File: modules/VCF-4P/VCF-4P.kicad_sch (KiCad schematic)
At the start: 40 parts, among them U1 SSI2140, U2 TL074

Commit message: VCF-4P: change a footprint
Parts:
- U1: footprint Package_SO:SSOP-20_4.4x6.5mm_P0.65mm -> (none)
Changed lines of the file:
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@@
       (effects (font (size 1.27 1.27)) hide)
     )
+    (pin "1")
+    (pin "2")
+    (pin "3")
+    (pin "5")
+    (pin "6")
+    (pin "7")
+    (pin "10")
+    (pin "8")
+    (pin "9")
     (pin "12")
     (pin "13")
     (pin "14")
+    (pin "11")
+    (pin "4")
   )
   (symbol (lib_id "-lmp:R_1%_0W166") (at 175.26 52.07 0) (unit 1)
@@
       (effects (font (size 1.27 1.27)) hide)
     )
+    (pin "1")
+    (pin "2")
+    (pin "3")
     (pin "5")
     (pin "6")
     (pin "7")
+    (pin "10")
+    (pin "8")
+    (pin "9")
+    (pin "12")
+    (pin "13")
+    (pin "14")
+    (pin "11")
+    (pin "4")
   )
   (symbol (lib_name "SSI2140_1") (lib_id "-lmp-synth:SSI2140") (at 106.68 152.4 0) (unit 6)
@@
       (effects (font (size 1.27 1.27)) (justify right))
     )
-    (property "Footprint" "Package_SO:SSOP-20_4.4x6.5mm_P0.65mm" (id 2) (at 112.395 141.605 0)
+    (property "Footprint" "" (id 2) (at 112.395 141.605 0)
       (effects (font (size 1.27 1.27)) hide)
     )
@@
       (effects (font (size 1.27 1.27)) hide)
     )
+    (pin "4")
+    (pin "5")
+    (pin "6")
+    (pin "1")
+    (pin "2")
+    (pin "3")
+    (pin "17")
+    (pin "18")
+    (pin "19")
+    (pin "14")
+    (pin "15")
+    (pin "16")
+    (pin "12")
+    (pin "13")
+    (pin "9")
     (pin "10")
     (pin "11")
@@
     (property "Reference" "U1" (id 0) (at 115.57 30.6664 0))
     (property "Value" "SSI2140" (id 1) (at 115.57 33.2033 0))
-    (property "Footprint" "Package_SO:SSOP-20_4.4x6.5mm_P0.65mm" (id 2) (at 120.015 28.575 0)
+    (property "Footprint" "" (id 2) (at 120.015 28.575 0)
       (effects (font (size 1.27 1.27)) hide)
     )
@@
     (pin "5")
     (pin "6")
+    (pin "1")
+    (pin "2")
+    (pin "3")
+    (pin "17")
+    (pin "18")
+    (pin "19")
+    (pin "14")
+    (pin "15")
+    (pin "16")
+    (pin "12")
+    (pin "13")
+    (pin "9")
+    (pin "10")
+    (pin "11")
+    (pin "20")
+    (pin "7")
+    (pin "8")
   )
   (symbol (lib_id "-lmp:R_1%_0W166") (at 91.44 52.07 0) (unit 1)
@@
     (property "Reference" "U1" (id 0) (at 189.23 30.6664 0))
     (property "Value" "SSI2140" (id 1) (at 189.23 33.2033 0))
-    (property "Footprint" "Package_SO:SSOP-20_4.4x6.5mm_P0.65mm" (id 2) (at 193.675 28.575 0)
+    (property "Footprint" "" (id 2) (at 193.675 28.575 0)
       (effects (font (size 1.27 1.27)) hide)
     )
@@
       (effects (font (size 1.27 1.27)) hide)
     )
+    (pin "4")
+    (pin "5")
+    (pin "6")
+    (pin "1")
+    (pin "2")
+    (pin "3")
     (pin "17")
     (pin "18")
     (pin "19")
+    (pin "14")
+    (pin "15")
+    (pin "16")
+    (pin "12")
+    (pin "13")
+    (pin "9")
+    (pin "10")
+    (pin "11")
+    (pin "20")
+    (pin "7")
+    (pin "8")
   )
   (symbol (lib_id "-lmp-synth:SSI2140") (at 151.13 39.37 0) (unit 2)
@@
     (property "Reference" "U1" (id 0) (at 152.4 30.6664 0))
     (property "Value" "SSI2140" (id 1) (at 152.4 33.2033 0))
-    (property "Footprint" "Package_SO:SSOP-20_4.4x6.5mm_P0.65mm" (id 2) (at 156.845 28.575 0)
+    (property "Footprint" "" (id 2) (at 156.845 28.575 0)
       (effects (font (size 1.27 1.27)) hide)
     )
@@
       (effects (font (size 1.27 1.27)) hide)
     )
+    (pin "4")
+    (pin "5")
+    (pin "6")
     (pin "1")
     (pin "2")
     (pin "3")
+    (pin "17")
+    (pin "18")
+    (pin "19")
+    (pin "14")
+    (pin "15")
+    (pin "16")
+    (pin "12")
+    (pin "13")
+    (pin "9")
+    (pin "10")
+    (pin "11")
+    (pin "20")
+    (pin "7")
+    (pin "8")
   )
   (symbol (lib_id "-lmp:R_1%_0W166") (at 138.43 52.07 0) (unit 1)
@@
     (property "Reference" "U1" (id 0) (at 101.6 66.1502 0))
     (property "Value" "SSI2140" (id 1) (at 101.6 68.6871 0))
-    (property "Footprint" "Package_SO:SSOP-20_4.4x6.5mm_P0.65mm" (id 2) (at 106.045 64.135 0)
+    (property "Footprint" "" (id 2) (at 106.045 64.135 0)
       (effects (font (size 1.27 1.27)) hide)
     )
@@
       (effects (font (size 1.27 1.27)) hide)
     )
+    (pin "4")
+    (pin "5")
+    (pin "6")
+    (pin "1")
+    (pin "2")
+    (pin "3")
+    (pin "17")
+    (pin "18")
+    (pin "19")
+    (pin "14")
+    (pin "15")
+    (pin "16")
     (pin "12")
     (pin "13")
     (pin "9")
+    (pin "10")
+    (pin "11")
+    (pin "20")
+    (pin "7")
+    (pin "8")
   )
   (symbol (lib_id "-lmp-power:GND") (at 212.09 57.15 0) (unit 1)
@@
     (property "Reference" "U1" (id 0) (at 226.06 30.6664 0))
     (property "Value" "SSI2140" (id 1) (at 226.06 33.2033 0))
-    (property "Footprint" "Package_SO:SSOP-20_4.4x6.5mm_P0.65mm" (id 2) (at 230.505 28.575 0)
+    (property "Footprint" "" (id 2) (at 230.505 28.575 0)
       (effects (font (size 1.27 1.27)) hide)
     )
@@
       (effects (font (size 1.27 1.27)) hide)
     )
+    (pin "4")
+    (pin "5")
+    (pin "6")
+    (pin "1")
+    (pin "2")
+    (pin "3")
+    (pin "17")
+    (pin "18")
+    (pin "19")
     (pin "14")
     (pin "15")
     (pin "16")
+    (pin "12")
+    (pin "13")
+    (pin "9")
+    (pin "10")
+    (pin "11")
+    (pin "20")
+    (pin "7")
+    (pin "8")
   )
   (symbol (lib_id "-lmp-opamp:TL074") (at 67.31 152.4 0) (mirror x) (unit 3)
@@
       (effects (font (size 1.27 1.27)) hide)
     )
+    (pin "1")
+    (pin "2")
+    (pin "3")
+    (pin "5")
+    (pin "6")
+    (pin "7")
     (pin "10")
     (pin "8")
     (pin "9")
+    (pin "12")
+    (pin "13")
+    (pin "14")
+    (pin "11")
+    (pin "4")
   )
   (symbol (lib_id "-lmp-synth:R_1K_Output") (at 222.25 102.87 90) (unit 1)
@@
     (pin "2")
     (pin "3")
+    (pin "5")
+    (pin "6")
+    (pin "7")
+    (pin "10")
+    (pin "8")
+    (pin "9")
+    (pin "12")
+    (pin "13")
+    (pin "14")
+    (pin "11")
+    (pin "4")
   )
   (symbol (lib_id "-lmp-power:GND") (at 58.42 157.48 0) (unit 1)
@@
     )
     (path "/35af1613-5429-4d36-8b84-d4f2f54bd286"
-      (reference "U1") (unit 1) (value "SSI2140") (footprint "Package_SO:SSOP-20_4.4x6.5mm_P0.65mm")
+      (reference "U1") (unit 1) (value "SSI2140") (footprint "-lmp-breakout:Breakout_DIP-20_W15.24mm")
     )
     (path "/7b9141a7-0442-4e17-91fc-6134d64028ce"
-      (reference "U1") (unit 2) (value "SSI2140") (footprint "Package_SO:SSOP-20_4.4x6.5mm_P0.65mm")
+      (reference "U1") (unit 2) (value "SSI2140") (footprint "-lmp-breakout:Breakout_DIP-20_W15.24mm")
     )
     (path "/799ca06d-feeb-42b5-93f5-6141a9976a1b"
-      (reference "U1") (unit 3) (value "SSI2140") (footprint "Package_SO:SSOP-20_4.4x6.5mm_P0.65mm")
+      (reference "U1") (unit 3) (value "SSI2140") (footprint "-lmp-breakout:Breakout_DIP-20_W15.24mm")
     )
     (path "/9773e1b2-867f-4bba-aab9-6aa389e51a1c"
-      (reference "U1") (unit 4) (value "SSI2140") (footprint "Package_SO:SSOP-20_4.4x6.5mm_P0.65mm")
+      (reference "U1") (unit 4) (value "SSI2140") (footprint "-lmp-breakout:Breakout_DIP-20_W15.24mm")
     )
     (path "/9131ee65-f6a7-4f4e-a019-faa937da667b"
-      (reference "U1") (unit 5) (value "SSI2140") (footprint "Package_SO:SSOP-20_4.4x6.5mm_P0.65mm")
+      (reference "U1") (unit 5) (value "SSI2140") (footprint "-lmp-breakout:Breakout_DIP-20_W15.24mm")
     )
     (path "/15b8c170-a65b-4a6d-a943-e95b801e6cde"
-      (reference "U1") (unit 6) (value "SSI2140") (footprint "Package_SO:SSOP-20_4.4x6.5mm_P0.65mm")
+      (reference "U1") (unit 6) (value "SSI2140") (footprint "-lmp-breakout:Breakout_DIP-20_W15.24mm")
     )
     (path "/d485a6e6-3ae5-4c97-8cc2-20d463f5a713"

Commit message: VCF-4P: input level uses audio-taper pot
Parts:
- U1: footprint (none) -> -lmp-breakout:Breakout_DIP-20_W15.24mm
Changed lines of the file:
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@@
       (effects (font (size 1.27 1.27)) (justify right))
     )
-    (property "Footprint" "" (id 2) (at 112.395 141.605 0)
+    (property "Footprint" "-lmp-breakout:Breakout_DIP-20_W15.24mm" (id 2) (at 112.395 141.605 0)
       (effects (font (size 1.27 1.27)) hide)
     )
@@
     (property "Reference" "U1" (id 0) (at 115.57 30.6664 0))
     (property "Value" "SSI2140" (id 1) (at 115.57 33.2033 0))
-    (property "Footprint" "" (id 2) (at 120.015 28.575 0)
+    (property "Footprint" "-lmp-breakout:Breakout_DIP-20_W15.24mm" (id 2) (at 120.015 28.575 0)
       (effects (font (size 1.27 1.27)) hide)
     )
@@
     (property "Reference" "U1" (id 0) (at 189.23 30.6664 0))
     (property "Value" "SSI2140" (id 1) (at 189.23 33.2033 0))
-    (property "Footprint" "" (id 2) (at 193.675 28.575 0)
+    (property "Footprint" "-lmp-breakout:Breakout_DIP-20_W15.24mm" (id 2) (at 193.675 28.575 0)
       (effects (font (size 1.27 1.27)) hide)
     )
@@
     (property "Reference" "U1" (id 0) (at 152.4 30.6664 0))
     (property "Value" "SSI2140" (id 1) (at 152.4 33.2033 0))
-    (property "Footprint" "" (id 2) (at 156.845 28.575 0)
+    (property "Footprint" "-lmp-breakout:Breakout_DIP-20_W15.24mm" (id 2) (at 156.845 28.575 0)
       (effects (font (size 1.27 1.27)) hide)
     )
@@
     (property "Reference" "U1" (id 0) (at 101.6 66.1502 0))
     (property "Value" "SSI2140" (id 1) (at 101.6 68.6871 0))
-    (property "Footprint" "" (id 2) (at 106.045 64.135 0)
+    (property "Footprint" "-lmp-breakout:Breakout_DIP-20_W15.24mm" (id 2) (at 106.045 64.135 0)
       (effects (font (size 1.27 1.27)) hide)
     )
@@
     (property "Reference" "U1" (id 0) (at 226.06 30.6664 0))
     (property "Value" "SSI2140" (id 1) (at 226.06 33.2033 0))
-    (property "Footprint" "" (id 2) (at 230.505 28.575 0)
-      (effects (font (size 1.27 1.27)) hide)
-    )
+    (property "Footprint" "-lmp-breakout:Breakout_DIP-20_W15.24mm" (id 2) (at 230.505 28.575 0)
+      (effects (font (size 1.27 1.27)) hide)
+    )

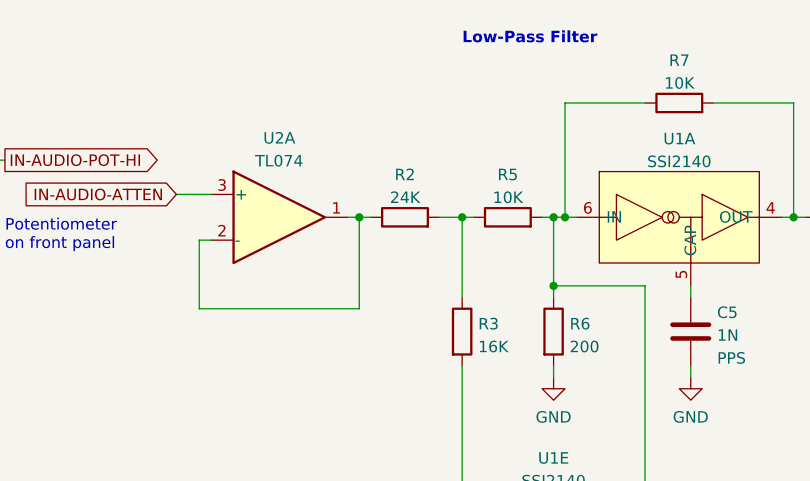
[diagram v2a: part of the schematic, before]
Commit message: VCF-4P: Breadboard prototype - wip
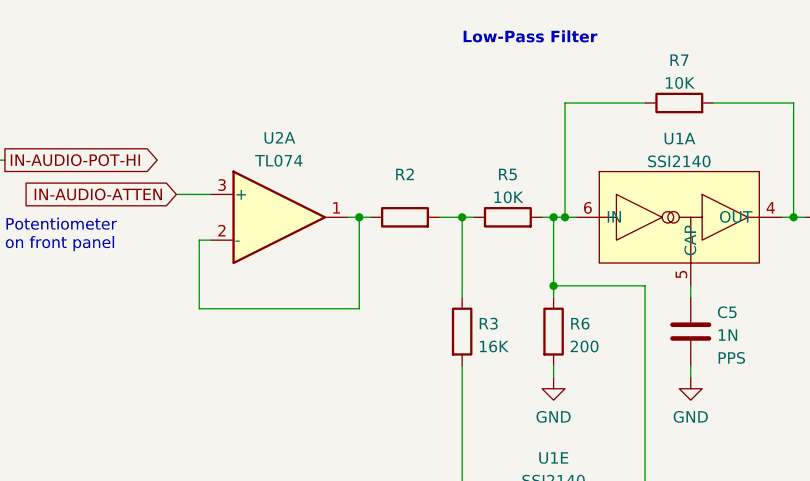
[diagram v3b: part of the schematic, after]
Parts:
- R2: value 24K -> (none); footprint -lmp-misc:R_Axial_DIN0207_L6.3mm_D2.5mm_P7.62mm_Horizontal -> (none)
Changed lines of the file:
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@@
     (in_bom yes) (on_board yes) (fields_autoplaced)
     (property "Reference" "R2" (id 0) (at 85.09 34.6542 90))
-    (property "Value" "24K" (id 1) (at 85.09 37.1911 90))
-    (property "Footprint" "-lmp-misc:R_Axial_DIN0207_L6.3mm_D2.5mm_P7.62mm_Horizontal" (id 2) (at 85.09 41.148 90)
+    (property "Value" "" (id 1) (at 85.09 37.1911 90))
+    (property "Footprint" "" (id 2) (at 85.09 41.148 90)
       (effects (font (size 1.27 1.27)) hide)
     )
@@
     )
     (path "/b1ba7b91-0010-48a5-9fd5-4fe0ea2e7c4f"
-      (reference "R2") (unit 1) (value "24K") (footprint "-lmp-misc:R_Axial_DIN0207_L6.3mm_D2.5mm_P7.62mm_Horizontal")
+      (reference "R2") (unit 1) (value "24K (15K?)") (footprint "-lmp-misc:R_Axial_DIN0207_L6.3mm_D2.5mm_P7.62mm_Horizontal")
     )
     (path "/3c085f79-ab56-4ae0-8f04-b1d322e8173a"
